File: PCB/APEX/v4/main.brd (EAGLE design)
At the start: 190.5 x 143.2 mm, 24 parts

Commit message: complete layout
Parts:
- removed JP10, JP11, JP4, JP5: (no value), microbuilder:1X06_ROUND_70
- removed JP2: (no value), microbuilder:1X05_ROUND_70
- removed JP7: (no value), microbuilder:1X07_ROUND_70
- removed PAD1, PAD2, PAD3, PAD4: (no value), wirepad:3,17/1,3
- added AMP: (no value), microbuilder:1X05_ROUND_70
- added BARO: (no value), microbuilder:1X07_ROUND_70
- added BNOCON, BNODAT, GPSDAT, GPSMOUNT: (no value), microbuilder:1X06_ROUND_70
- added SENS-GND, SENS-SCL, SENS-SDA, SENS-VCC: (no value), wirepad:3,17/1,3
- moved CON-SCL 179.5 mm to (68.6, 61.0)
- moved CON-GND 171.7 mm to (68.6, 64.8)
- moved CON-SDA 170.6 mm to (68.6, 57.1)
- moved CON-VCC 169.5 mm to (68.6, 68.6)
- moved EXTGND 157.4 mm to (73.7, 61.0), turned to 90 degrees
- moved SIMRHS 157.2 mm to (27.9, 82.5)
- moved EXTV+ 151.5 mm to (73.7, 57.1), turned to 90 degrees
- moved SIMLHS 144.7 mm to (27.9, 76.2)
- moved SIMISO 138.1 mm to (73.7, 67.3), turned to 270 degrees
- moved TINYRHS 132.9 mm to (62.2, 59.7), turned to 270 degrees
- moved TINYLHS 121.0 mm to (47.0, 59.7), turned to 90 degrees
- moved BAT 115.6 mm to (68.6, 52.1), turned to 270 degrees
- moved A1 95.5 mm to (54.6, 69.8), flipped to the bottom, turned to 270 degrees
- moved U$1 93.7 mm to (30.6, 60.2), flipped to the bottom
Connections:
- net N$1 renamed TX
- net N$2 renamed RX
- net !RESET: now also GPSDAT.6; no longer JP10.6
- net 1PPS: now also GPSMOUNT.2; no longer JP11.2
- net 3.3V_2: now also BARO.2; no longer JP7.2
- net 3.3V_3: now also GPSDAT.2; no longer JP10.2
- net 3.3V_BNO: now also BNODAT.2; no longer JP4.2
- net AIN+: now also AMP.5; no longer JP2.5
- net BOOT: now also BNOCON.1; no longer JP5.1
- net CS: now also BNOCON.6; no longer JP5.6
- net CS_BARO: now also BARO.7; no longer JP7.7
- net GND: now also AMP.1, AMP.4, BARO.3, BNOCON.2, BNOCON.3, BNODAT.3, GPSDAT.3, GPSMOUNT.1, SENS-GND.1; no longer JP10.3, JP11.1, JP2.1, JP2.4, JP4.3, JP5.2, JP5.3, JP7.3
- net INT: now also BNODAT.6; no longer JP4.6
- net MOSI: now also BNOCON.5; no longer JP5.5
- net RXI: now also GPSMOUNT.4; no longer JP11.4
- net SCL: now also BARO.4, BNODAT.4, GPSDAT.4, SENS-SCL.1; no longer JP10.4, JP4.4, JP7.4, PAD3.1
- net SDA: now also BARO.6, BNODAT.5, GPSDAT.5, SENS-SDA.1; no longer JP10.5, JP4.5, JP7.6, PAD4.1
- net SDO/ADR: now also BARO.5; no longer JP7.5
- net TXO: now also GPSMOUNT.5; no longer JP11.5
- net VCC: now also AMP.2, BARO.1, BNOCON.4, BNODAT.1, GPSDAT.1, GPSMOUNT.3, SENS-VCC.1; no longer JP10.1, JP11.3, JP2.2, JP4.1, JP5.4, JP7.1
- net WAKEUP: now also GPSMOUNT.6; no longer JP11.6
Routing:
- net SIMPOW: track 0.00 -> 59.0 mm
- net VCC: track 0.00 -> 20.0 mm
- net GND: track 0.00 -> 19.7 mm
- net TX: track 0.00 -> 5.46 mm
- net RX: track 0.00 -> 5.45 mm
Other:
- board size 190.5 x 143.2 mm -> 68.7 x 51.8 mm

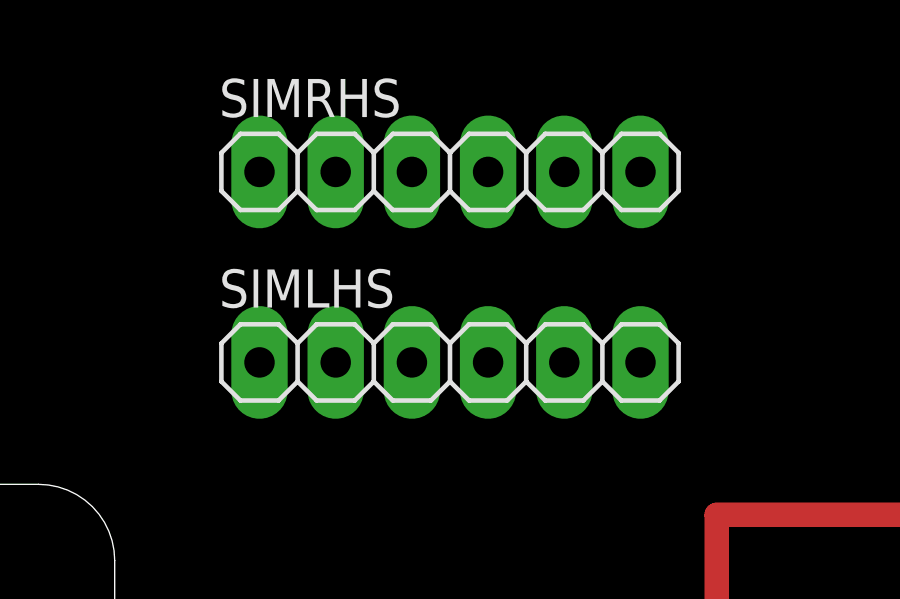
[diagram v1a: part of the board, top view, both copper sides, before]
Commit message: use drc to increase pad size
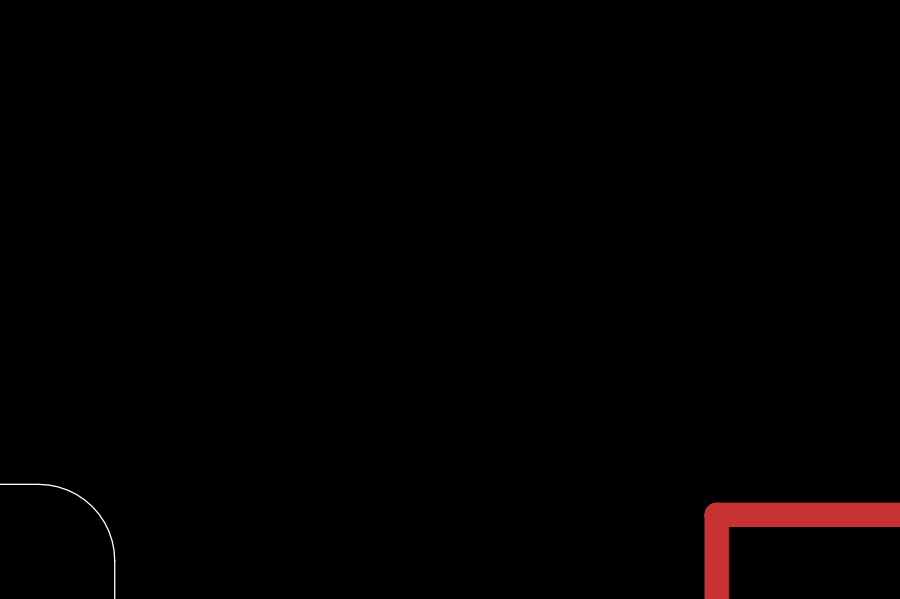
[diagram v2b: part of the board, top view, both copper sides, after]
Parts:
- removed SIMLHS, SIMRHS: (no value), pinhead:1X06
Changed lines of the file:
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@@
 <attribute name="VALUE" x="59.055" y="69.85" size="1.27" layer="27" rot="R270"/>
-</element>
-<element name="SIMLHS" library="pinhead" library_urn="urn:adsk.eagle:library:325" package="1X06" package3d_urn="urn:adsk.eagle:package:22472/2" value="" x="27.94" y="76.2" smashed="yes">
-<attribute name="NAME" x="20.2438" y="78.0288" size="1.27" layer="25" ratio="10"/>
-<attribute name="POPULARITY" value="79" x="27.94" y="76.2" size="1.778" layer="27" display="off"/>
-<attribute name="VALUE" x="20.32" y="73.025" size="1.27" layer="27"/>
-</element>
-<element name="SIMRHS" library="pinhead" library_urn="urn:adsk.eagle:library:325" package="1X06" package3d_urn="urn:adsk.eagle:package:22472/2" value="" x="27.94" y="82.55" smashed="yes">
-<attribute name="NAME" x="20.2438" y="84.3788" size="1.27" layer="25" ratio="10"/>
-<attribute name="POPULARITY" value="79" x="27.94" y="82.55" size="1.778" layer="27" display="off"/>
-<attribute name="VALUE" x="20.32" y="79.375" size="1.27" layer="27"/>
 </element>
 <element name="EXTV+" library="wirepad" library_urn="urn:adsk.eagle:library:412" package="SMD2,54-5,08" package3d_urn="urn:adsk.eagle:package:30841/1" value="" x="73.66" y="57.15" smashed="yes" rot="R90">
